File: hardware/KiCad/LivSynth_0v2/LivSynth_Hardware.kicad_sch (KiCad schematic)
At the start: 0 parts

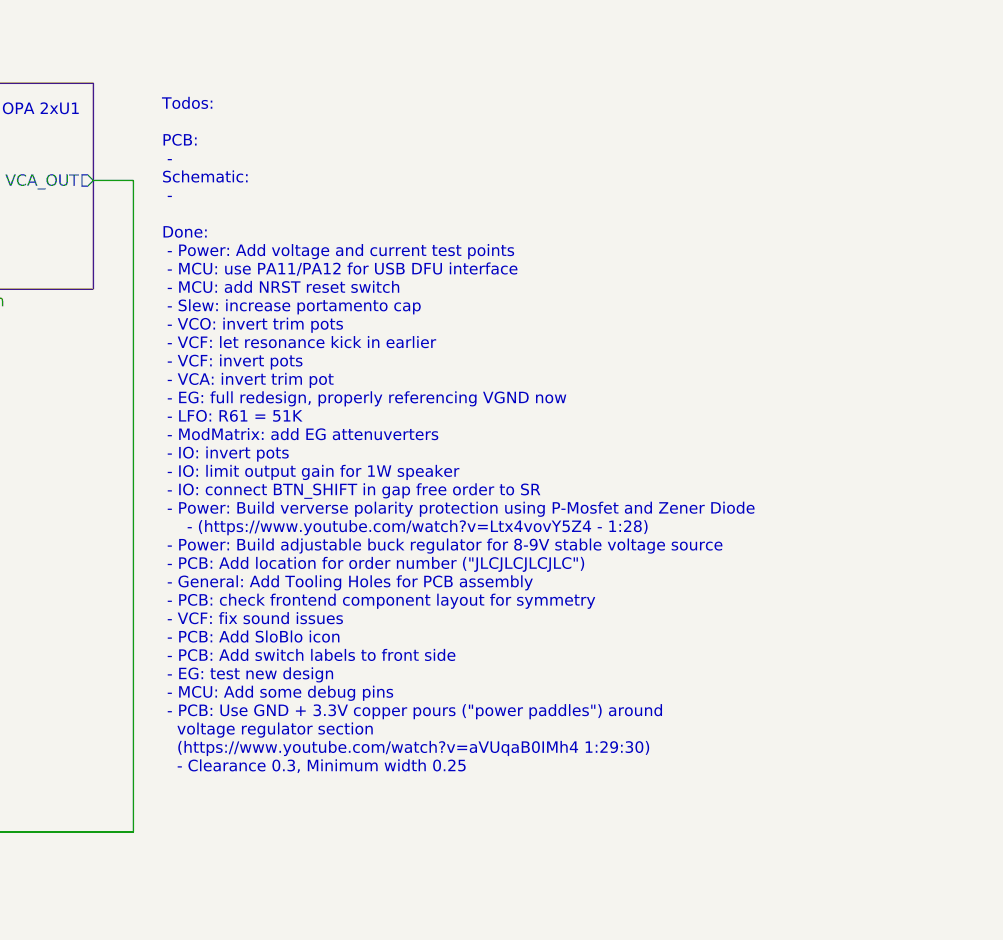
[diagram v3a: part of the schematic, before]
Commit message: Reduce EG cap to 4u7 Reduce LFO cap to 220n VCO R23: 470K, C13: 10n
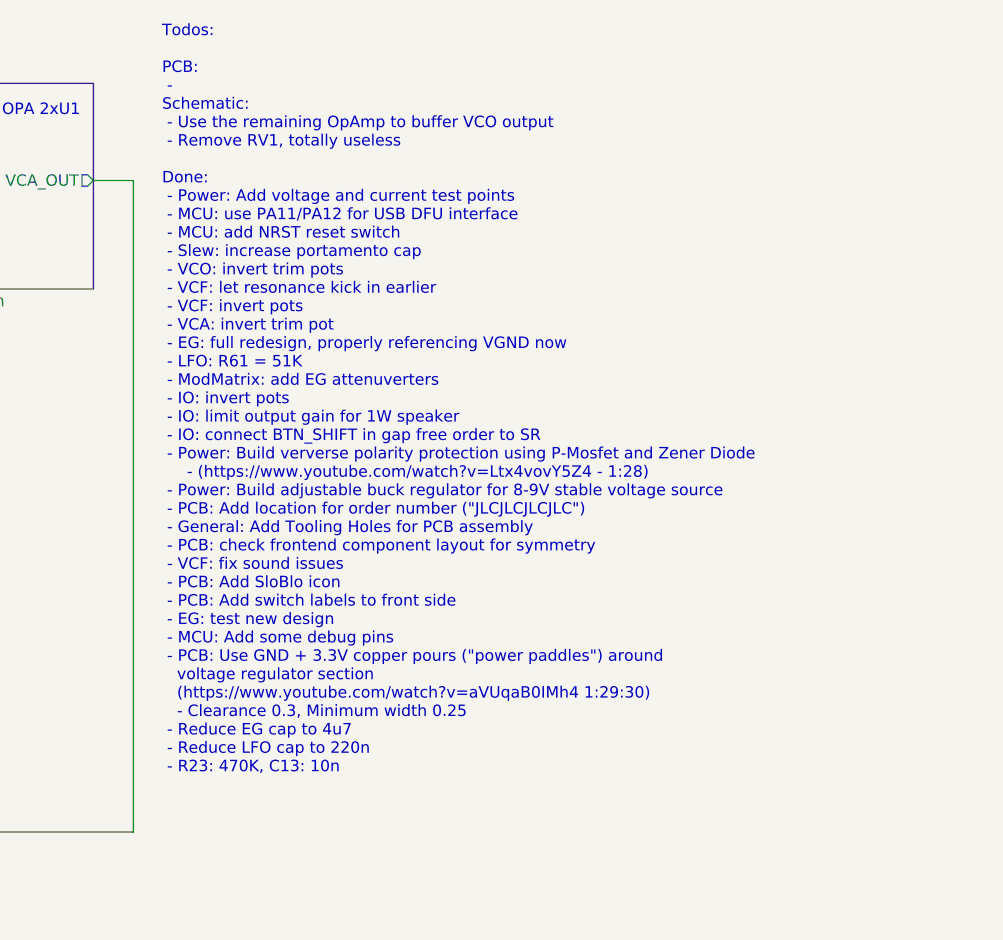
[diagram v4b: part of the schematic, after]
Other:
- note added: "Todos: PCB: - Schematic: - Use the remaining OpAmp to buffer VCO output - Remove RV1, totally useless Done: - Power: Add voltage and current test points - MCU: use PA11/PA12 for USB DFU interface - MCU: add NRST reset switch - Slew: increase portamento cap - VCO: invert trim pots - VCF: let resonance kick in earlier - VCF: invert pots - VCA: invert trim pot - EG: full redesign, properly referenci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"
- note removed: "Todos: PCB: - Schematic: - Done: - Power: Add voltage and current test points - MCU: use PA11/PA12 for USB DFU interface - MCU: add NRST reset switch - Slew: increase portamento cap - VCO: invert trim pots - VCF: let resonance kick in earlier - VCF: invert pots - VCA: invert trim pot - EG: full redesign, properly referencing VGND now - LFO: R61 = 51K - ModMatrix: add EG attenuverters - IO: invert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"

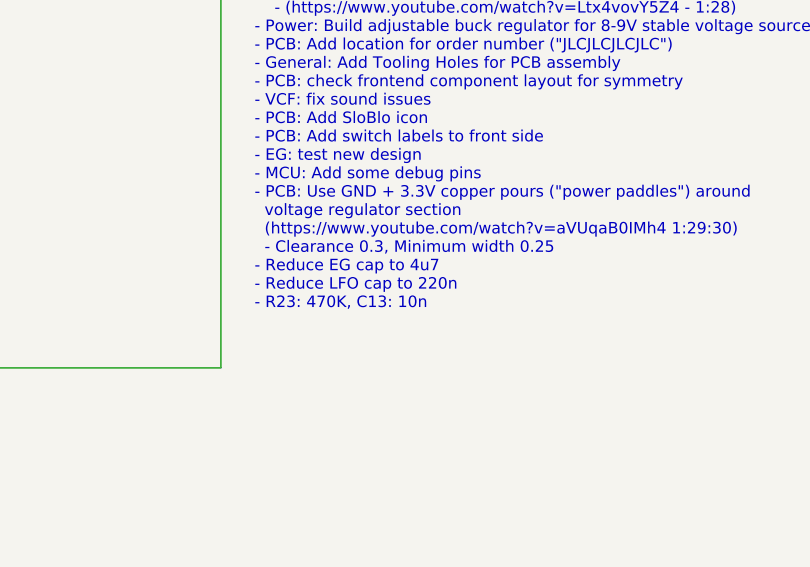
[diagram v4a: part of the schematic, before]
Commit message: EG: raise Rf of comparator circuit to improve performance LFO: raise coupling resistor for higher amplitude, adapt cap for more musical ranges
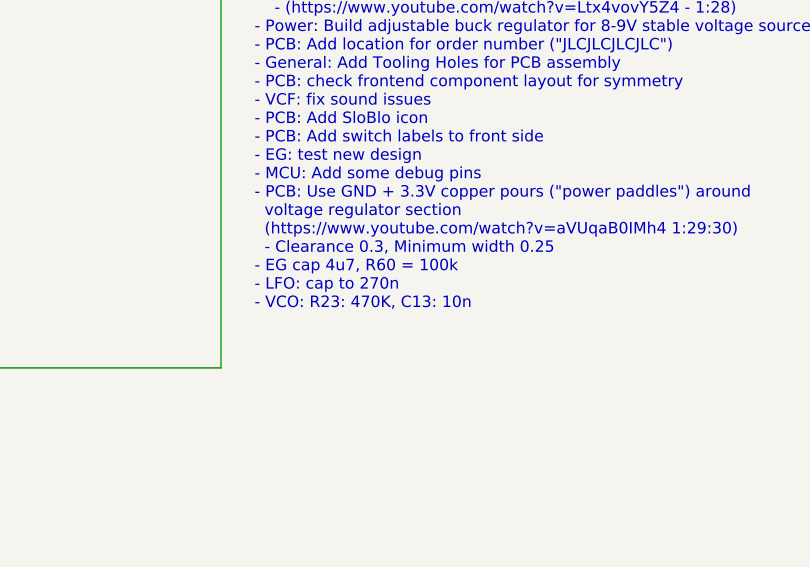
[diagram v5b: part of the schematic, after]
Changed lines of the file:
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@@
     (effects (font (size 1.27 1.27)) (justify left bottom))
   )
-  (text "Todos:\n\nPCB:\n - \nSchematic:\n - Use the remaining OpAmp to buffer VCO output\n - Remove RV1, totally useless\n\nDone:\n - Power: Add voltage and current test points\n - MCU: use PA11/PA12 for USB DFU interface\n - MCU: add NRST reset switch\n - Slew: increase portamento cap\n - VCO: invert trim pots\n - VCF: let resonance kick in earlier\n - VCF: invert pots\n - VCA: invert trim pot\n - EG: full redesign, properly referencing VGND now\n - LFO: R61 = 51K\n - ModMatrix: add EG attenuverters\n - IO: invert pots\n - IO: limit output gain for 1W speaker\n - IO: connect BTN_SHIFT in gap free order to SR\n - Power: Build ververse polarity protection using P-Mosfet and Zener Diode\n     - (https://www.youtube.com/watch?v=Ltx4vovY5Z4 - 1:28)\n - Power: Build adjustable buck regulator for 8-9V stable voltage source\n - PCB: Add location for order number (\"JLCJLCJLCJLC\")\n - General: Add Tooling Holes for PCB assembly\n - PCB: check frontend component layout for symmetry\n - VCF: fix sound issues\n - PCB: Add SloBlo icon\n - PCB: Add switch labels to front side\n - EG: test new design\n - MCU: Add some debug pins\n - PCB: Use GND + 3.3V copper pours (\"power paddles\") around\n   voltage regulator section\n   (https://www.youtube.com/watch?v=aVUqaB0IMh4 1:29:30)\n   - Clearance 0.3, Minimum width 0.25\n - Reduce EG cap to 4u7\n - Reduce LFO cap to 220n\n - R23: 470K, C13: 10n"
+  (text "Todos:\n\nPCB:\n - \nSchematic:\n - Use the remaining OpAmp to buffer VCO output\n - Remove RV1, totally useless\n\nDone:\n - Power: Add voltage and current test points\n - MCU: use PA11/PA12 for USB DFU interface\n - MCU: add NRST reset switch\n - Slew: increase portamento cap\n - VCO: invert trim pots\n - VCF: let resonance kick in earlier\n - VCF: invert pots\n - VCA: invert trim pot\n - EG: full redesign, properly referencing VGND now\n - LFO: R61 = 51K\n - ModMatrix: add EG attenuverters\n - IO: invert pots\n - IO: limit output gain for 1W speaker\n - IO: connect BTN_SHIFT in gap free order to SR\n - Power: Build ververse polarity protection using P-Mosfet and Zener Diode\n     - (https://www.youtube.com/watch?v=Ltx4vovY5Z4 - 1:28)\n - Power: Build adjustable buck regulator for 8-9V stable voltage source\n - PCB: Add location for order number (\"JLCJLCJLCJLC\")\n - General: Add Tooling Holes for PCB assembly\n - PCB: check frontend component layout for symmetry\n - VCF: fix sound issues\n - PCB: Add SloBlo icon\n - PCB: Add switch labels to front side\n - EG: test new design\n - MCU: Add some debug pins\n - PCB: Use GND + 3.3V copper pours (\"power paddles\") around\n   voltage regulator section\n   (https://www.youtube.com/watch?v=aVUqaB0IMh4 1:29:30)\n   - Clearance 0.3, Minimum width 0.25\n - EG cap 4u7, R60 = 100k\n - LFO: cap to 270n\n - VCO: R23: 470K, C13: 10n"
     (at 212.09 99.695 0)
     (effects (font (size 1.27 1.27)) (justify left bottom))
